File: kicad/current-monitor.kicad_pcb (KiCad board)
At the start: 2 copper layers, 55.2 x 21 mm, 29 parts, among them J1 Conn_01x02_Male, J2 Conn_01x02_Male, J3 Conn_02x05_Top_Bottom, U1 SIT1602BI-21-XXE-8.192000G, U2 MIC5504-3.3YM5

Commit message: snapshot
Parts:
- added H1: MountingHole, MountingHole:MountingHole_2.2mm_M2_Pad_Via, F.Cu at (142.0, 103.0)
- added H2: MountingHole, MountingHole:MountingHole_2.2mm_M2_Pad_Via, F.Cu at (174.0, 117.0)
- added I1: INA381, HH_TexasInstruments:INA381-WSON, F.Cu at (151.8, 114.8)
- added I2: INA381, HH_TexasInstruments:INA381-WSON, F.Cu at (151.8, 118.0)
- added R12: 2, Resistor_SMD:R_0612_1632Metric, F.Cu at (147.2, 116.5)
- C7: moved to B.Cu
- J1, J2: value Conn_01x02_Male -> Conn_02x02_Odd_Even; footprint Connector_PinHeader_2.54mm:PinHeader_1x02_P2.54mm_Vertical_SMD_Pin1Left -> Connector_PinHeader_2.54mm:PinHeader_2x02_P2.54mm_Vertical_SMD
- J3: value Conn_02x05_Top_Bottom -> Conn_02x05_Odd_Even
- R1: footprint Resistor_SMD:R_0603_1608Metric -> Resistor_SMD:R_0612_1632Metric
- moved C9 32.4 mm to (163.3, 118.2), turned to 180 degrees
- moved C8 30.8 mm to (163.3, 115.6), turned to 180 degrees
- moved U2 23.5 mm to (167.7, 117.1), turned to 180 degrees
- moved J2 13.6 mm to (139.5, 116.8), turned to 0 degrees
- moved J1 8.84 mm to (139.5, 109.8), turned to 0 degrees
- moved C10 7.92 mm to (163.5, 112.8), turned to 90 degrees
- moved J3 5.48 mm to (176.2, 107.0)
- moved R2 5.00 mm to (153.8, 110.0)
- moved C7 4.82 mm to (167.2, 105.2), turned to 0 degrees
- moved Z1 4.75 mm to (151.0, 109.8)
- moved U1 4.55 mm to (166.8, 112.8), turned to 0 degrees
- moved R6 3.80 mm to (156.2, 106.5)
- moved C2 3.75 mm to (158.9, 105.8)
- moved R3 3.75 mm to (153.8, 105.0)
- moved R7 3.75 mm to (156.2, 105.0)
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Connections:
- J1 pad 1: /sensors/S1- -> GND
- J1 pad 2: GND -> /sensors/S1-
- J2 pad 1: /sensors/S1+ -> GND
- J2 pad 2: GND -> /sensors/S3-
- J3 pad 2: /adc/CIPO -> /adc/GND
- J3 pad 3: /adc/SCLK -> /adc/CIPO
- J3 pad 4: /adc/~CS -> /power/5V
- J3 pad 5: /adc/~DRDY -> /adc/SCLK
- J3 pad 6: /adc/GND -> /adc/3V3
- J3 pad 7: /power/5V -> /adc/~CS
- J3 pad 8: /adc/3V3 -> /adc/GND
- J3 pad 9: /adc/GND -> /adc/~DRDY
- R1 pad 1: /sensors/S1- -> /sensors/S1+
- R1 pad 2: /sensors/S1+ -> /sensors/S1-
- R10 pad 2: (no net) -> /sensors/OUT4
- R4 pad 2: /sensors/OUT1 -> (no net)
- R6 pad 2: /sensors/OUT2 -> (no net)
- R8 pad 2: (no net) -> /sensors/OUT3
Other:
- board size 55.2 x 21 mm -> 50 x 20 mm

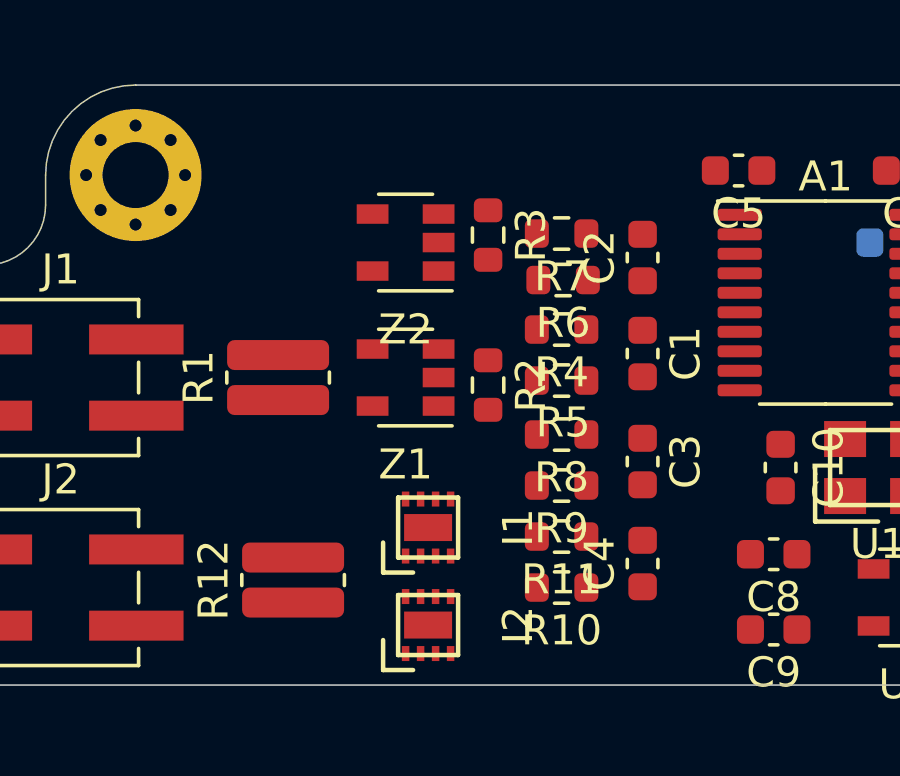
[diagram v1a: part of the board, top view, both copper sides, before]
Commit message: add second R_sense
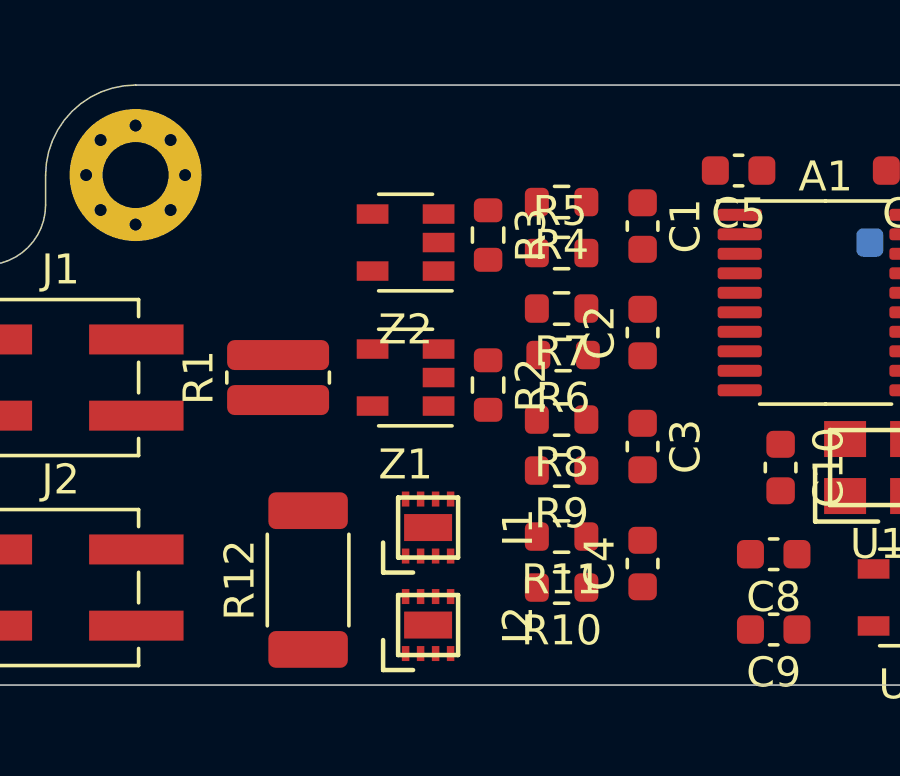
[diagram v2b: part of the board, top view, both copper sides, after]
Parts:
- added L1: logo, HH_Hochreiner:logo, B.Cu at (158.0, 110.0)
- R12: value 2 -> .4; footprint Resistor_SMD:R_0612_1632Metric -> Resistor_SMD:R_2010_5025Metric
- moved C1 4.25 mm to (158.9, 104.7)
- moved R4 4.25 mm to (156.2, 103.9)
- moved R5 4.25 mm to (156.2, 105.6), turned to 180 degrees
- moved C2 2.50 mm to (158.9, 108.2)
- moved R6 2.50 mm to (156.2, 109.0)
- moved R7 2.50 mm to (156.2, 107.5)
- moved C3 0.50 mm to (158.9, 112.0)
- moved R12 0.50 mm to (147.8, 116.5)
- moved R8 0.50 mm to (156.2, 111.2)
- moved R9 0.50 mm to (156.2, 112.8)
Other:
- board text added: "current-monitor V1.0.0 hochreiner.net"

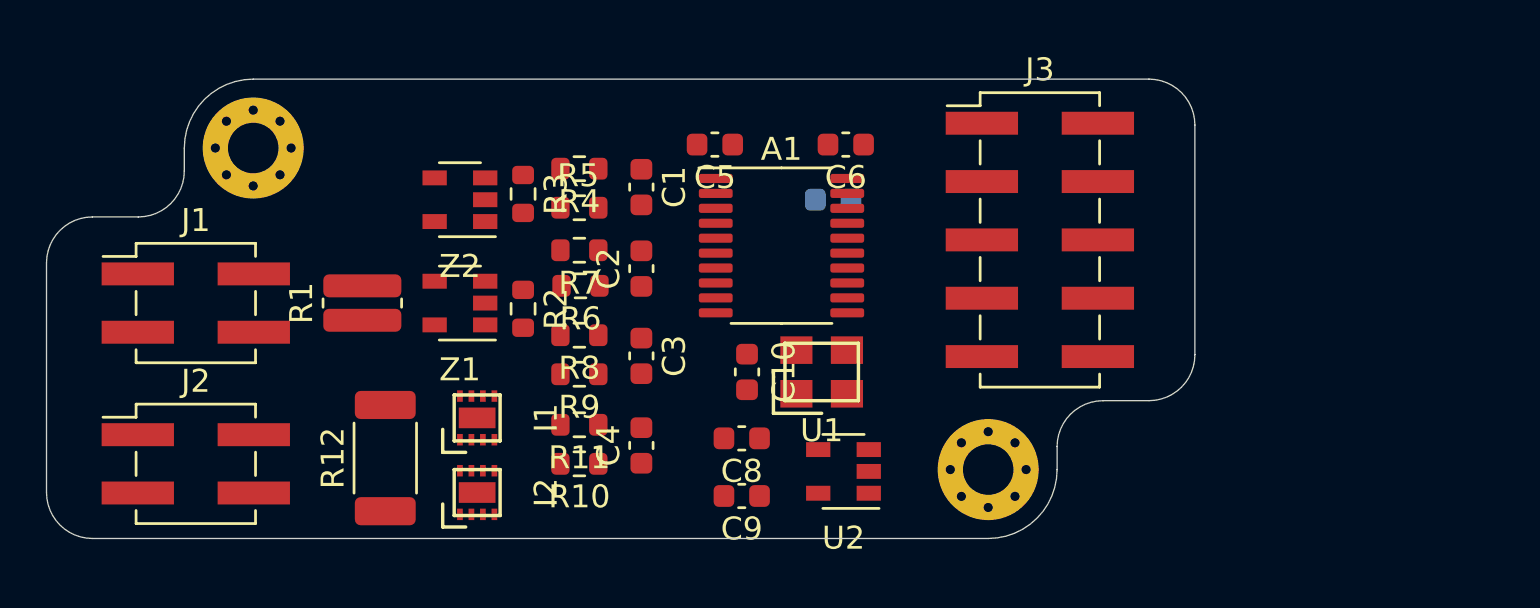
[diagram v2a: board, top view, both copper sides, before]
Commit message: move clock to back
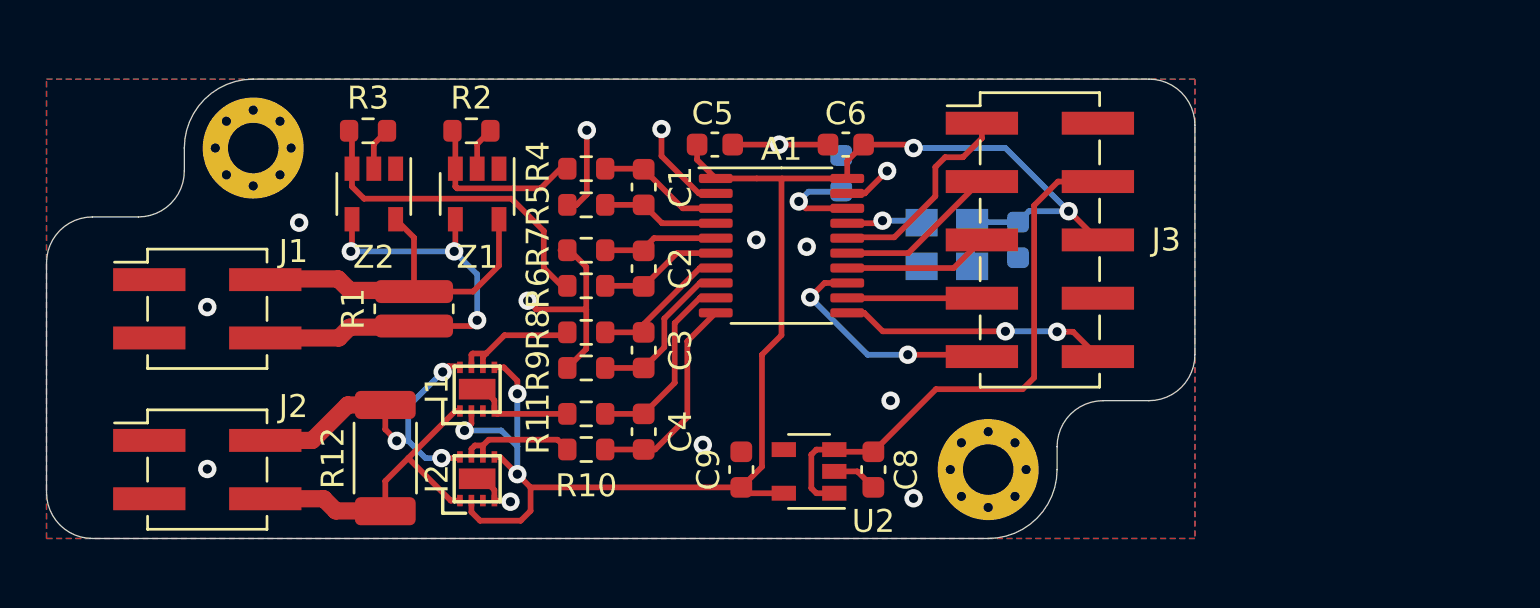
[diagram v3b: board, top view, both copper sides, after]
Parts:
- C10, U1: moved to B.Cu
- moved C10 13.1 mm to (175.3, 107.0), turned to 270 degrees
- moved R2 8.07 mm to (151.5, 102.2), turned to 0 degrees
- moved U1 7.78 mm to (172.2, 107.2), turned to 180 degrees
- moved R3 7.29 mm to (147.0, 102.2), turned to 0 degrees
- moved C8 5.89 mm to (169.0, 117.0), turned to 270 degrees
- moved Z1 4.81 mm to (151.8, 105.0), turned to 270 degrees
- moved Z2 3.76 mm to (147.2, 105.0), turned to 270 degrees
- moved R1 2.26 mm to (149.0, 110.0)
- moved U2 1.50 mm to (166.2, 117.1)
- moved I1 1.25 mm to (151.8, 113.5)
- moved C7 1.20 mm to (167.6, 104.1), turned to 270 degrees
- moved C9 1.15 mm to (163.2, 117.0), turned to 90 degrees
- moved R10 0.69 mm to (156.5, 116.1)
- moved C4 0.61 mm to (159.0, 115.3)
- moved I2 0.60 mm to (151.8, 117.4)
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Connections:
- A1 pad 19: /adc/GND -> GND
- A1 pad 2: /adc/GND -> GND
- C10 pad 2: /adc/GND -> GND
- C5 pad 1: /adc/GND -> GND
- C6 pad 2: /adc/GND -> GND
- C7 pad 1: /adc/GND -> GND
- C8 pad 2: /adc/GND -> GND
- C9 pad 2: /adc/GND -> GND
- I1 pad 4: /adc/GND -> GND
- I1 pad PAD: /adc/GND -> GND
- I2 pad 4: /adc/GND -> GND
- I2 pad PAD: /adc/GND -> GND
- J3 pad 2: /adc/GND -> GND
- J3 pad 8: /adc/GND -> GND
- R11 pad 2: /adc/GND -> GND
- R2 pad 2: /adc/GND -> GND
- R3 pad 2: /adc/GND -> GND
- R4 pad 2: (no net) -> /sensors/OUT1
- R5 pad 2: /adc/GND -> GND
- R6 pad 2: (no net) -> /sensors/OUT2
- R7 pad 2: /adc/GND -> GND
- R9 pad 2: /adc/GND -> GND
- U1 pad 2: /adc/GND -> GND
- U2 pad 2: /adc/GND -> GND
- Z1 pad 2: /adc/GND -> GND
- Z2 pad 2: /adc/GND -> GND
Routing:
- net /adc/3V3: track 0.00 -> 68.3 mm, vias 0 -> 5
- net GND: track 0.00 -> 35.7 mm, vias 0 -> 14
- net /power/5V: track 0.00 -> 24.4 mm
- net /sensors/S1+: track 0.00 -> 20.4 mm, vias 0 -> 3
- net /sensors/S1-: track 0.00 -> 16.4 mm
- net /sensors/S3-: track 0.00 -> 15.2 mm, vias 0 -> 3
- net /sensors/OUT2: track 0.00 -> 14.3 mm
- net /sensors/S3+: track 0.00 -> 14.3 mm
- net /adc/~SYNC: track 0.00 -> 11.7 mm, vias 0 -> 2
- net /adc/~DRDY: track 0.00 -> 10.4 mm, vias 0 -> 2
- net Net-(A1-Pad10): track 0.00 -> 9.22 mm
- net /adc/COPI: track 0.00 -> 9.09 mm
- net Net-(A1-Pad9): track 0.00 -> 8.43 mm
- net /sensors/OUT1: track 0.00 -> 7.44 mm
- net /adc/CIPO: track 0.00 -> 7.15 mm
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- added copper zone on B.Cu, net GND
- added copper zone on F.Cu, net GND

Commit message: put markings on pcb
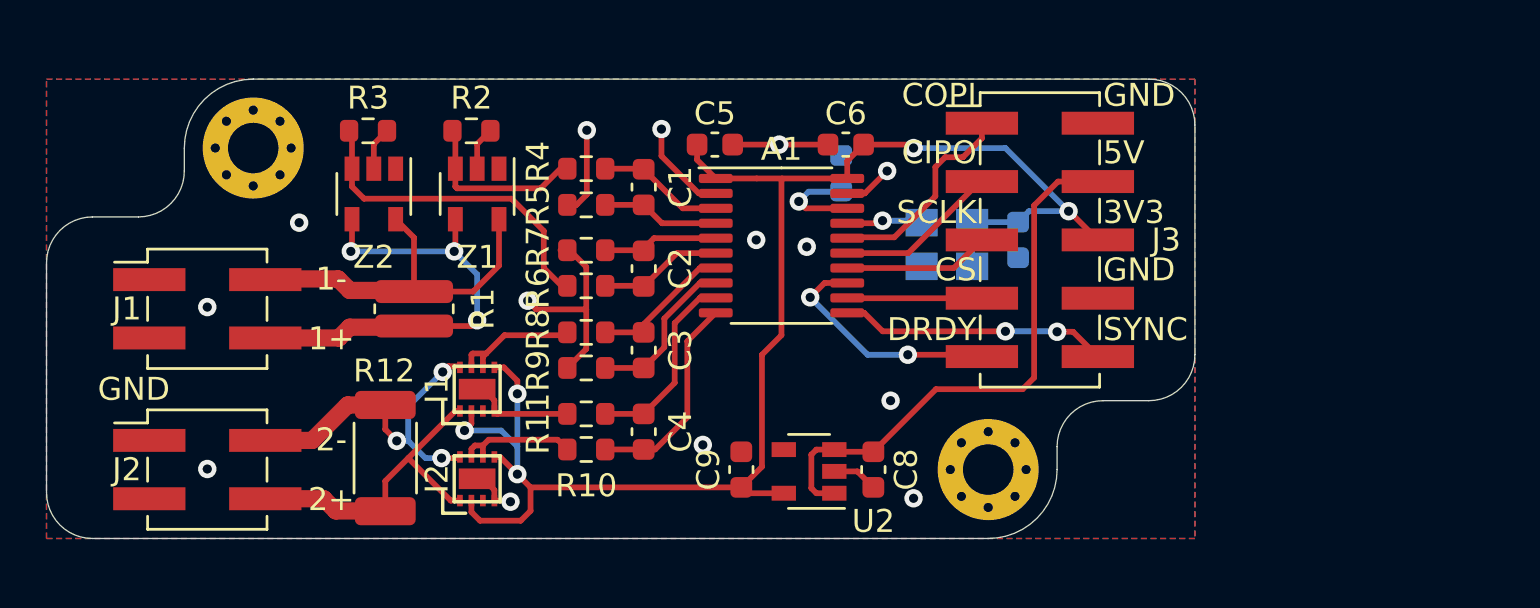
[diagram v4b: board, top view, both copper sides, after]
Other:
- board text added: "1+"
- board text added: "1-"
- board text added: "2+"
- board text added: "2-"
- board text added: "3V3"
- board text added: "5V"
- board text added: "CIPO"
- board text added: "COPI"
- board text added: "CS"
- board text added: "DRDY"
- board text added: "GND"
- board text added: "SCLK"
- board text added: "SYNC"

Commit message: switch clock and add bypass
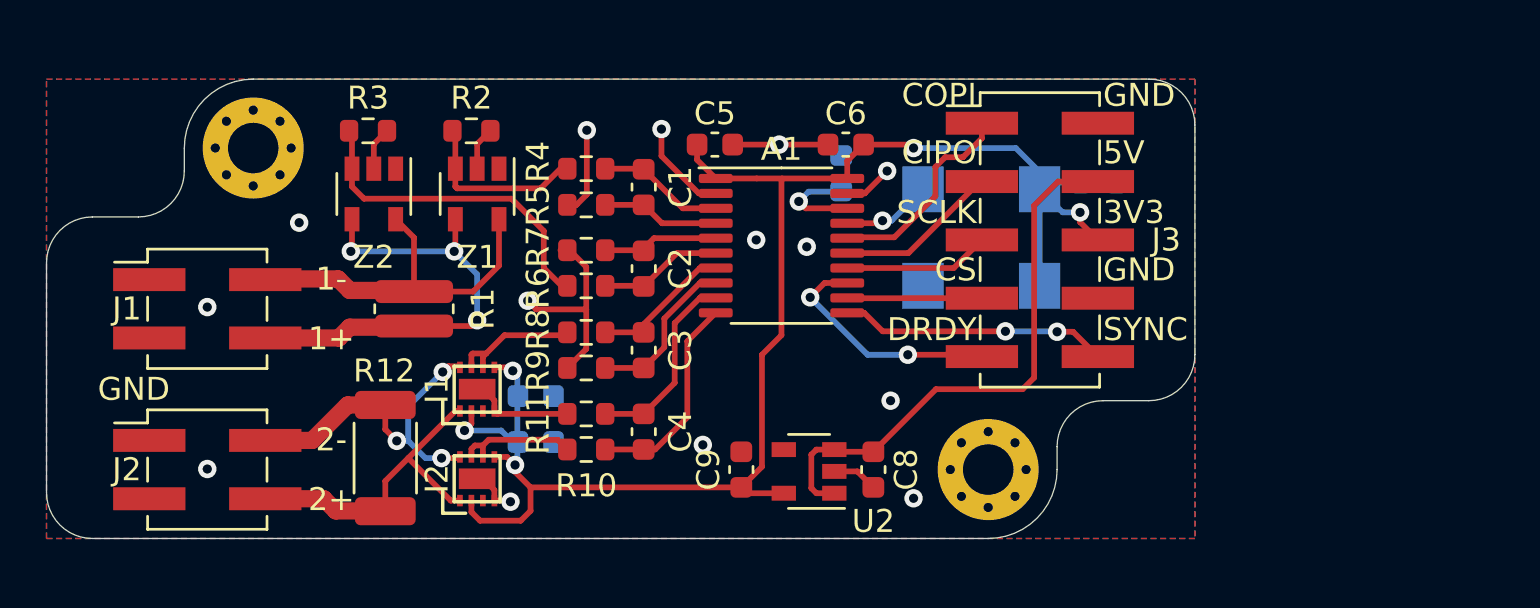
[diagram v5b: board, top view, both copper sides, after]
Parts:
- added C11: 0.1µF X7R 0603, Capacitor_SMD:C_0603_1608Metric, B.Cu at (154.3, 113.8)
- added C12: 0.1µF X7R 0603, Capacitor_SMD:C_0603_1608Metric, B.Cu at (154.3, 115.8)
- C1, C2, C3, C4: value 10nF -> 10nF C0G 0603
- C10: value 0.1µF -> 0.1µF X7R 0603
- C5, C6: value 1µF -> 1µF X7R 0603
- C7: value 220nF -> 220nF X7R 0603
- R10, R11, R2, R3, R4, R5, R6, R7, R8, R9: value 1k -> 1k 1% 0603 0.3W
- U1: value SIT1602BI-21-XXE-8.192000G -> CB3LV-3I-8M192000; footprint HH_SiTime:SIT1602BI-21-XXE-8.192000G -> HH_CTS-FrequencyControls:CB3LV-3I-8M192000
- moved C10 4.30 mm to (178.8, 104.5), turned to 180 degrees
- moved L1 4.00 mm to (162.0, 110.0)
- moved U1 1.53 mm to (173.7, 106.9)
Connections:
- C10 pad 1: /adc/3V3 -> GND
- C10 pad 2: GND -> /adc/3V3
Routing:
- net Net-(A1-Pad17): track 3.32 -> 3.91 mm
